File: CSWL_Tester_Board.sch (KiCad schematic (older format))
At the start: 169 parts, among them J1 DB9_Female ID09S33E4GV00LF, J10 Conn_01x03_Male, J11 Conn_01x02, J12 Conn_01x02, J13 Conn_01x02, J14 Conn_01x04, J15 SPI1, J16 Conn_02x10_Odd_Even, J17 Conn_01x02, J18 Conn_01x02, J19 Conn_01x02, J2 Conn_01x04, J20 Conn_01x02, J21 Fix hole, J22 Conn_01x02, J23 Conn_01x03, J24 Conn_01x02, J25 USB_B_Micro, J26 Conn_01x04, J27 Conn_01x10, J28 Fix hole, J29 Fix hole, J3 Conn_01x04, J30 Fix hole, J31 Conn_Coaxial_Power, J4 Conn_01x04, J5 DB9_Female ID09S33E4GV00LF, J6 Conn_01x04, J7 Conn_01x04, J8 DB9_Female ID09S33E4GV00LF, J9 Conn_Coaxial_Power, K1 G6SU-2 DC5, K2 G6SU-2 DC5, K3 G6SU-2 DC5, K4 G6SU-2 DC5, K5 G6SU-2 DC5, Q1 DMG2301L, Q10 2N7002LT1G, Q11 2N7002LT1G, Q2 DMG2301L, Q3 DMG2301L, Q4 2N7002LT1G, Q5 2N7002LT1G, Q6 2N7002LT1G, Q7 DMG2301L, Q8 DMG2301L, U1 MAX3221EIPW, U10 EL817-S1-A (NC), U2 STM32F103RCT6, U3 MAX3221EIPW, U4 MCP1700T-3302E_TT, U5 MAX3221EIPW, U6 EL817-S1-A (NC), U7 EL817-S1-A (NC), U8 EL817-S1-A (NC), U9 EL817-S1-A (NC), Y1 8MHz

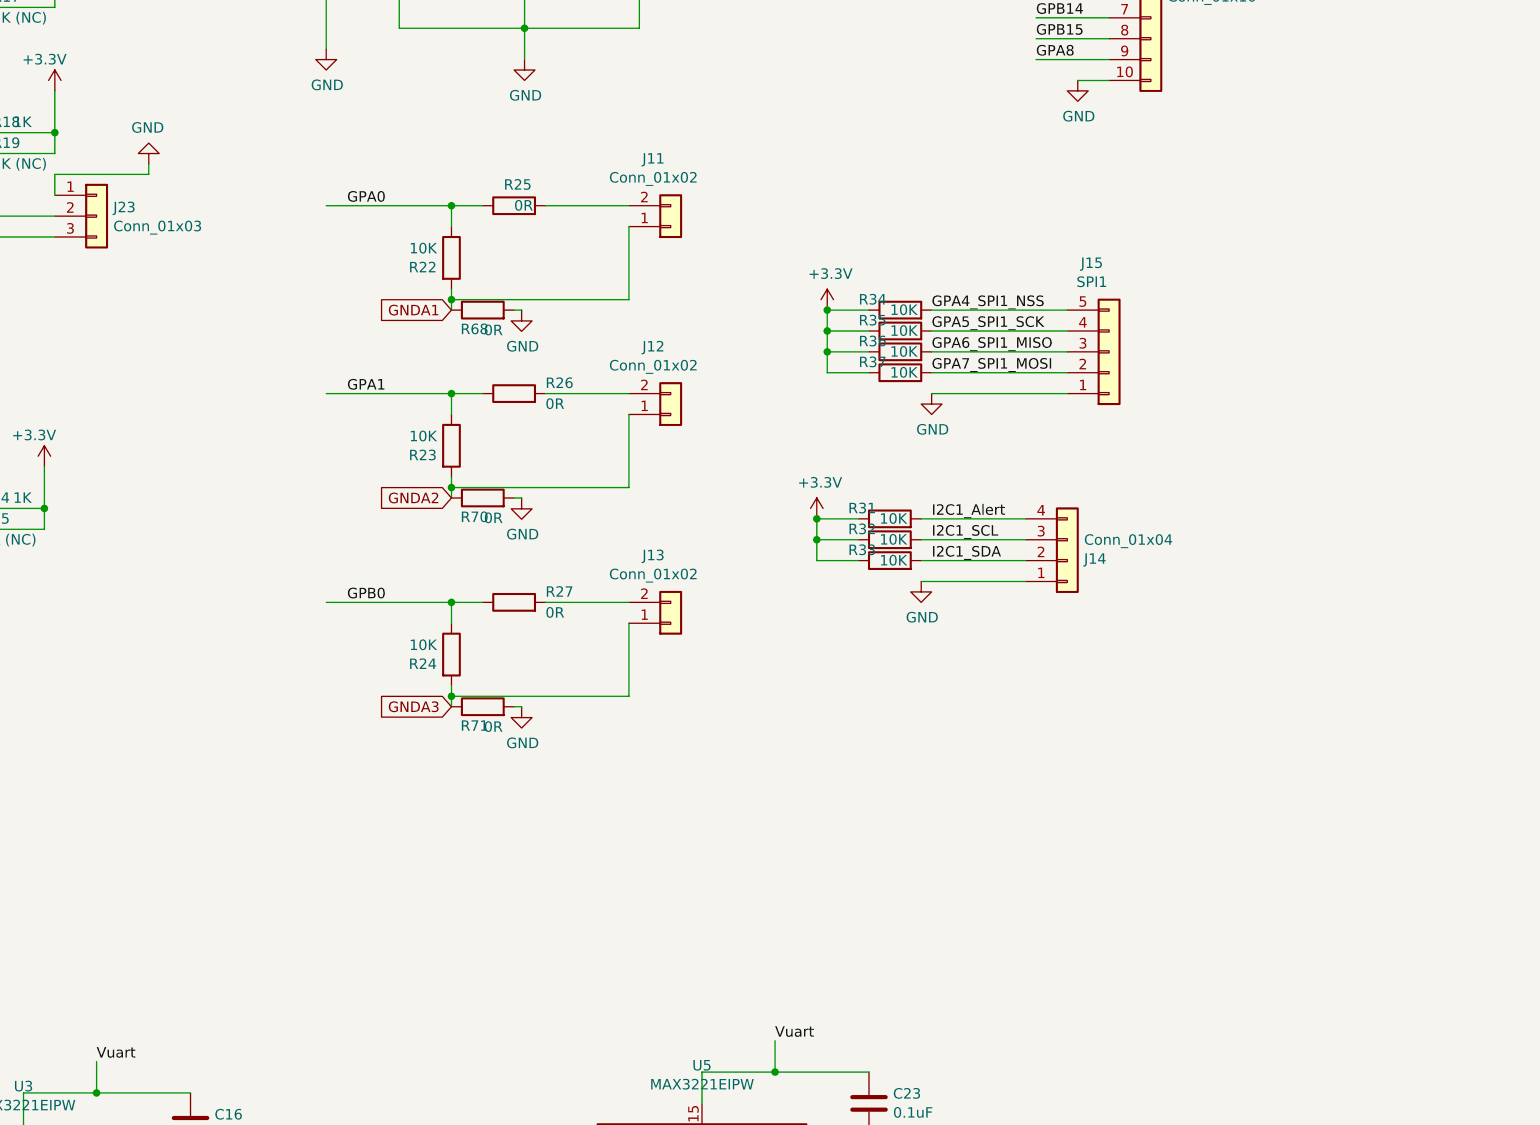
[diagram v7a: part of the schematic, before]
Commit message: Ruan: add more function on ADC connector
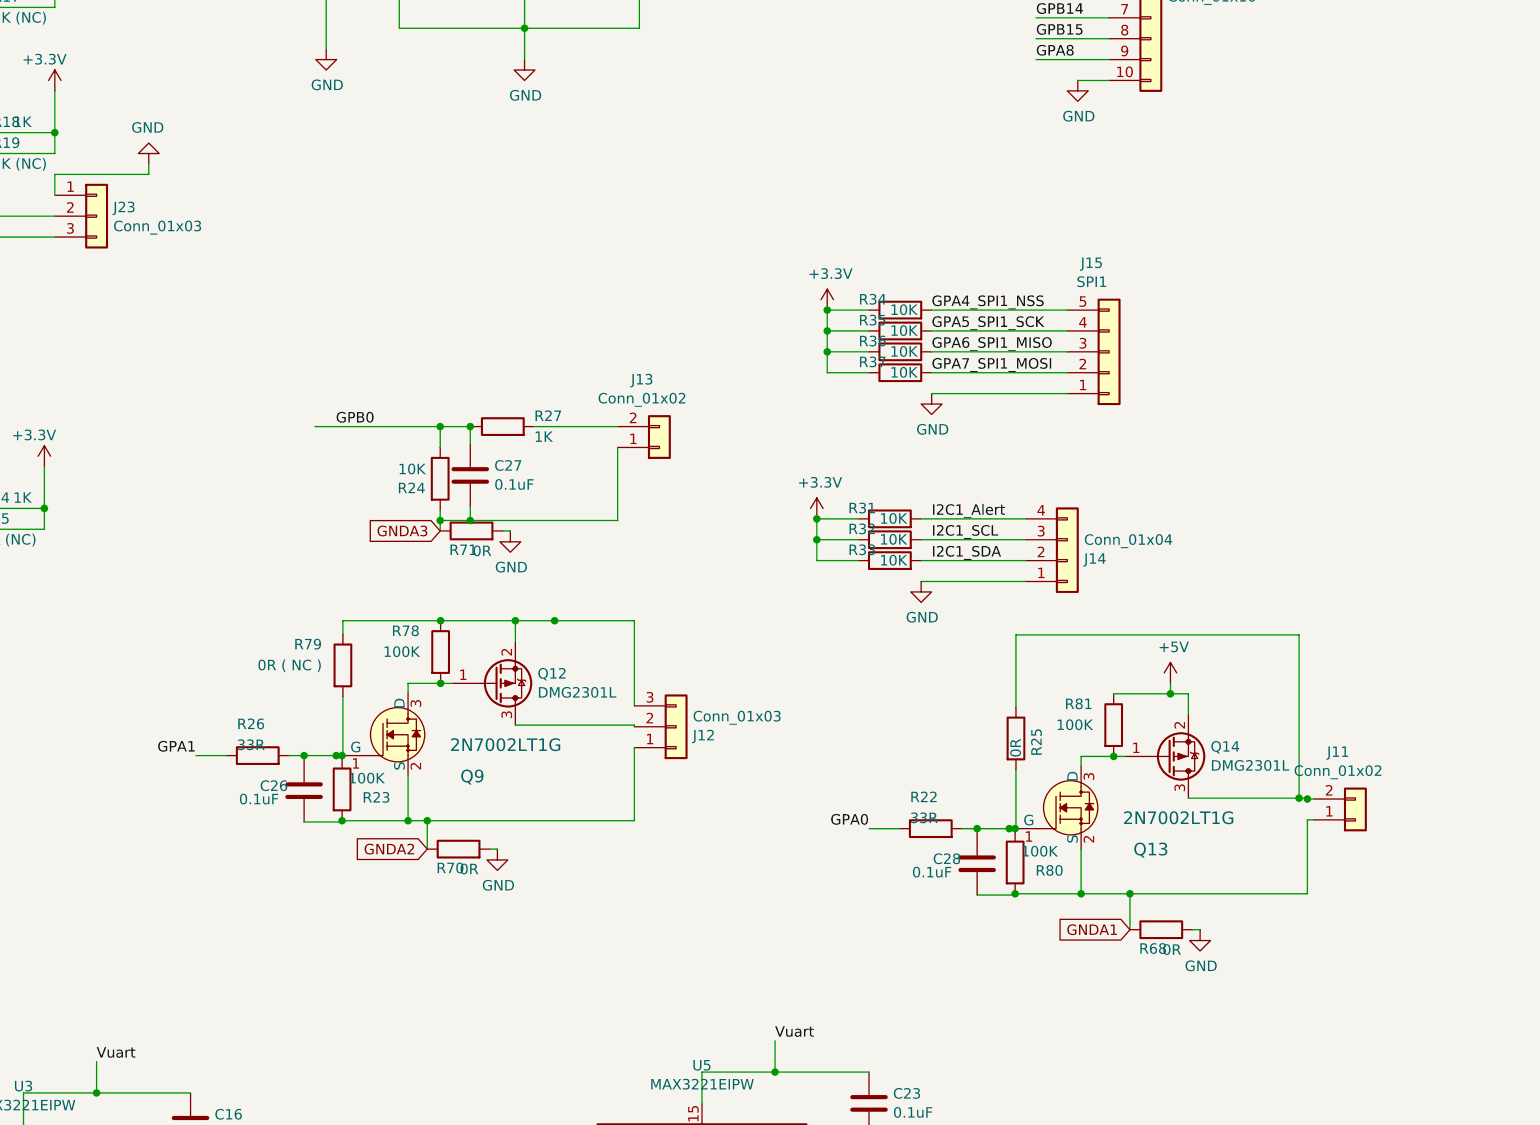
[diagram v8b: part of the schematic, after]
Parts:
- removed J12: Conn_01x02, RuanProject:Connector_Set_1x02_P2.54mm_Vertical, symbol Connector_Generic:Conn_01x02
- added C26, C27, C28: 0.1uF, Capacitor_SMD:C_0603_1608Metric, symbol Device:C
- added J12: Conn_01x03, RuanProject:Connector_Set_1x03_P2.54mm_Vertical, symbol Connector_Generic:Conn_01x03
- added Q12, Q14: DMG2301L, Package_TO_SOT_SMD:SOT-23, symbol Transistor_FET:DMG2301L
- added Q13, Q9: 2N7002LT1G, digikey-footprints:SOT-23-3, symbol dk_Transistors-FETs-MOSFETs-Single:2N7002LT1G
- added R78, R80, R81: 100K, Resistor_SMD:R_0603_1608Metric, symbol Device:R
- added R79: 0R ( NC ), Resistor_SMD:R_0603_1608Metric, symbol Device:R
- R22: value 10K -> 33R
- R23: value 10K -> 100K
- R26: value 0R -> 33R
- R27: value 0R -> 1K
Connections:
- wire segments 600 -> 653
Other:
- moved on the sheet: J11, J13, R23, R24, R25, R27, R68, R70, R71
